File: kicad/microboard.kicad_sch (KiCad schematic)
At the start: 12 parts, among them J2 to microboard, J3 to baseboard, Q1 AH3712-P-B, U3 HT7550, U5 LM35-LP

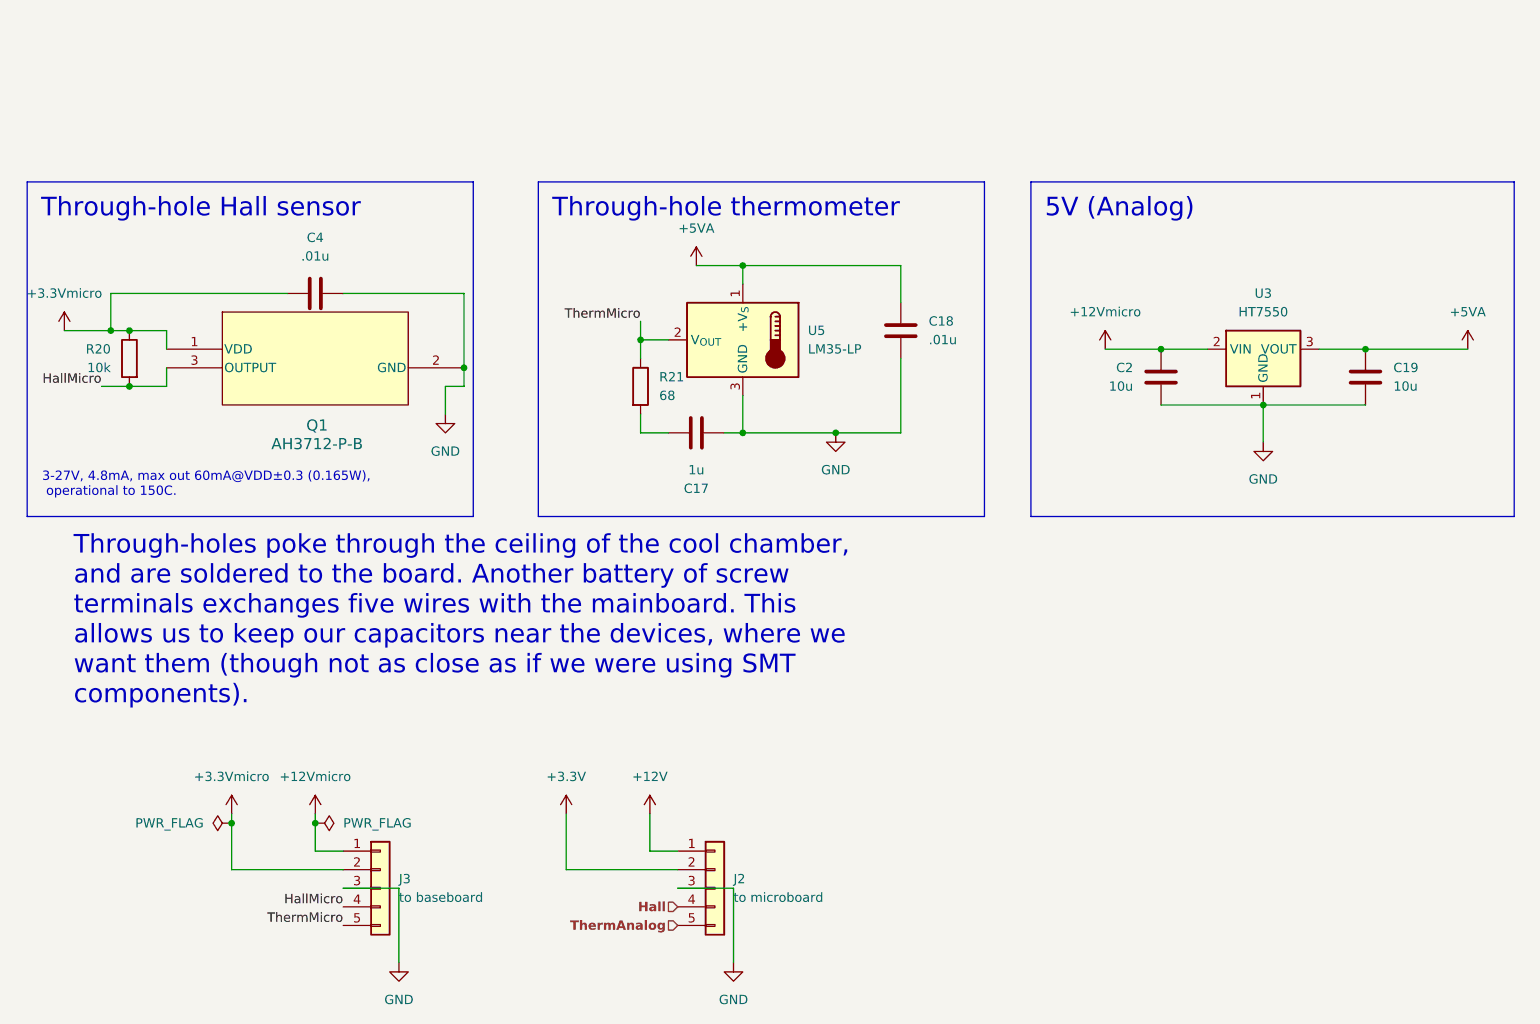
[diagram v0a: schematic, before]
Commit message: call ledc_fade_func_install(). call setup_adc_oneshot() after setup_temp()
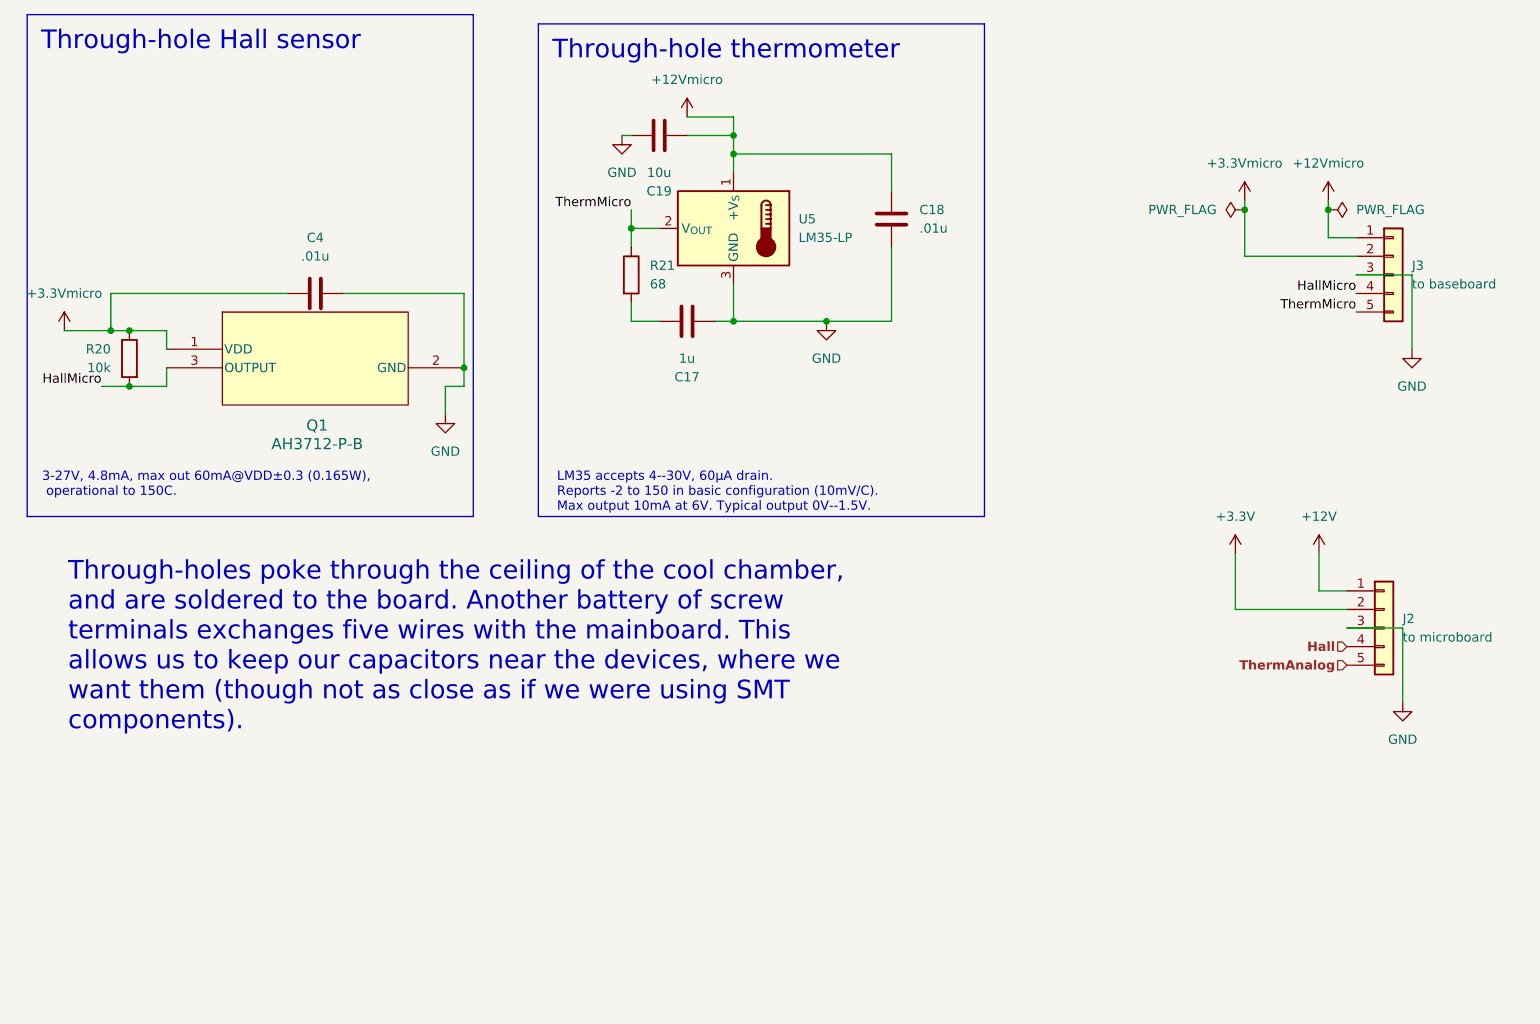
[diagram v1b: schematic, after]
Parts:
- removed C2: 10u, Capacitor_SMD:C_0805_2012Metric_Pad1.18x1.45mm_HandSolder, symbol Device:C
- removed U3: HT7550, Package_TO_SOT_SMD:SOT-89-3, symbol Regulator_Linear:HT75xx-1-SOT89
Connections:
- net +12Vmicro: now also C18.1, C19.2, U5.1 (+V_{S})
- net GND: now also C19.1; no longer C19.2
- removed net +5VA: C18.1, C19.1, U5.1 (+V_{S})
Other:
- note added: "LM35 accepts 4--30V, 60µA drain. Reports -2 to 150 in basic configuration (10mV/C). Max output 10mA at 6V. Typical output 0V--1.5V."
- moved on the sheet: C17, C18, C19, J2, J3, R21, U5

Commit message: [schematics] sync to grid
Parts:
- C18, C4: value .01u -> 10n
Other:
- note added: "Through-holes poke through the ceiling of the cool chamber, and are soldered to the board. A JST connector exchanges five wires with the mainboard. This allows us to keep our capacitors near the devices, where we want them (though not as close as if we were using SMT components)."
- note removed: "Through-holes poke through the ceiling of the cool chamber, and are soldered to the board. Another battery of screw terminals exchanges five wires with the mainboard. This allows us to keep our capacitors near the devices, where we want them (though not as close as if we were using SMT components)."
- moved on the sheet: C17, C18, C19, C4, Q1, R20, R21, U5

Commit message: [kicad] tighten things up
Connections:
- net +3.3V: now also J2.3 (Pin_3); no longer J2.2 (Pin_2)
- net +3.3Vmicro: now also J3.3 (Pin_3); no longer J3.2 (Pin_2)
- net GND: now also J2.2 (Pin_2), J3.2 (Pin_2); no longer J2.3 (Pin_3), J3.3 (Pin_3)

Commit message: put your boot down
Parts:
- C17, C18, C19, C4: footprint Capacitor_SMD:C_0805_2012Metric_Pad1.18x1.45mm_HandSolder -> Capacitor_SMD:C_1206_3216Metric_Pad1.33x1.80mm_HandSolder
- R20, R21: footprint Resistor_SMD:R_0805_2012Metric_Pad1.20x1.40mm_HandSolder -> Resistor_SMD:R_1206_3216Metric_Pad1.30x1.75mm_HandSolder
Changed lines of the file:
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@@
 			)
 		)
-		(property "Footprint" "Resistor_SMD:R_0805_2012Metric_Pad1.20x1.40mm_HandSolder"
+		(property "Footprint" "Resistor_SMD:R_1206_3216Metric_Pad1.30x1.75mm_HandSolder"
 			(at 117.602 71.12 90)
 			(effects
@@
 			)
 		)
-		(property "Footprint" "Resistor_SMD:R_0805_2012Metric_Pad1.20x1.40mm_HandSolder"
+		(property "Footprint" "Resistor_SMD:R_1206_3216Metric_Pad1.30x1.75mm_HandSolder"
 			(at 51.308 63.5 90)
 			(effects
@@
 			)
 		)
-		(property "Footprint" "Capacitor_SMD:C_0805_2012Metric_Pad1.18x1.45mm_HandSolder"
+		(property "Footprint" "Capacitor_SMD:C_1206_3216Metric_Pad1.33x1.80mm_HandSolder"
 			(at 153.9748 67.31 0)
 			(effects
@@
 			)
 		)
-		(property "Footprint" "Capacitor_SMD:C_0805_2012Metric_Pad1.18x1.45mm_HandSolder"
+		(property "Footprint" "Capacitor_SMD:C_1206_3216Metric_Pad1.33x1.80mm_HandSolder"
 			(at 127 53.0352 0)
 			(effects
@@
 			)
 		)
-		(property "Footprint" "Capacitor_SMD:C_0805_2012Metric_Pad1.18x1.45mm_HandSolder"
+		(property "Footprint" "Capacitor_SMD:C_1206_3216Metric_Pad1.33x1.80mm_HandSolder"
 			(at 71.12 53.6448 0)
 			(effects
@@
 			)
 		)
-		(property "Footprint" "Capacitor_SMD:C_0805_2012Metric_Pad1.18x1.45mm_HandSolder"
+		(property "Footprint" "Capacitor_SMD:C_1206_3216Metric_Pad1.33x1.80mm_HandSolder"
 			(at 130.81 78.4352 0)
 			(effects

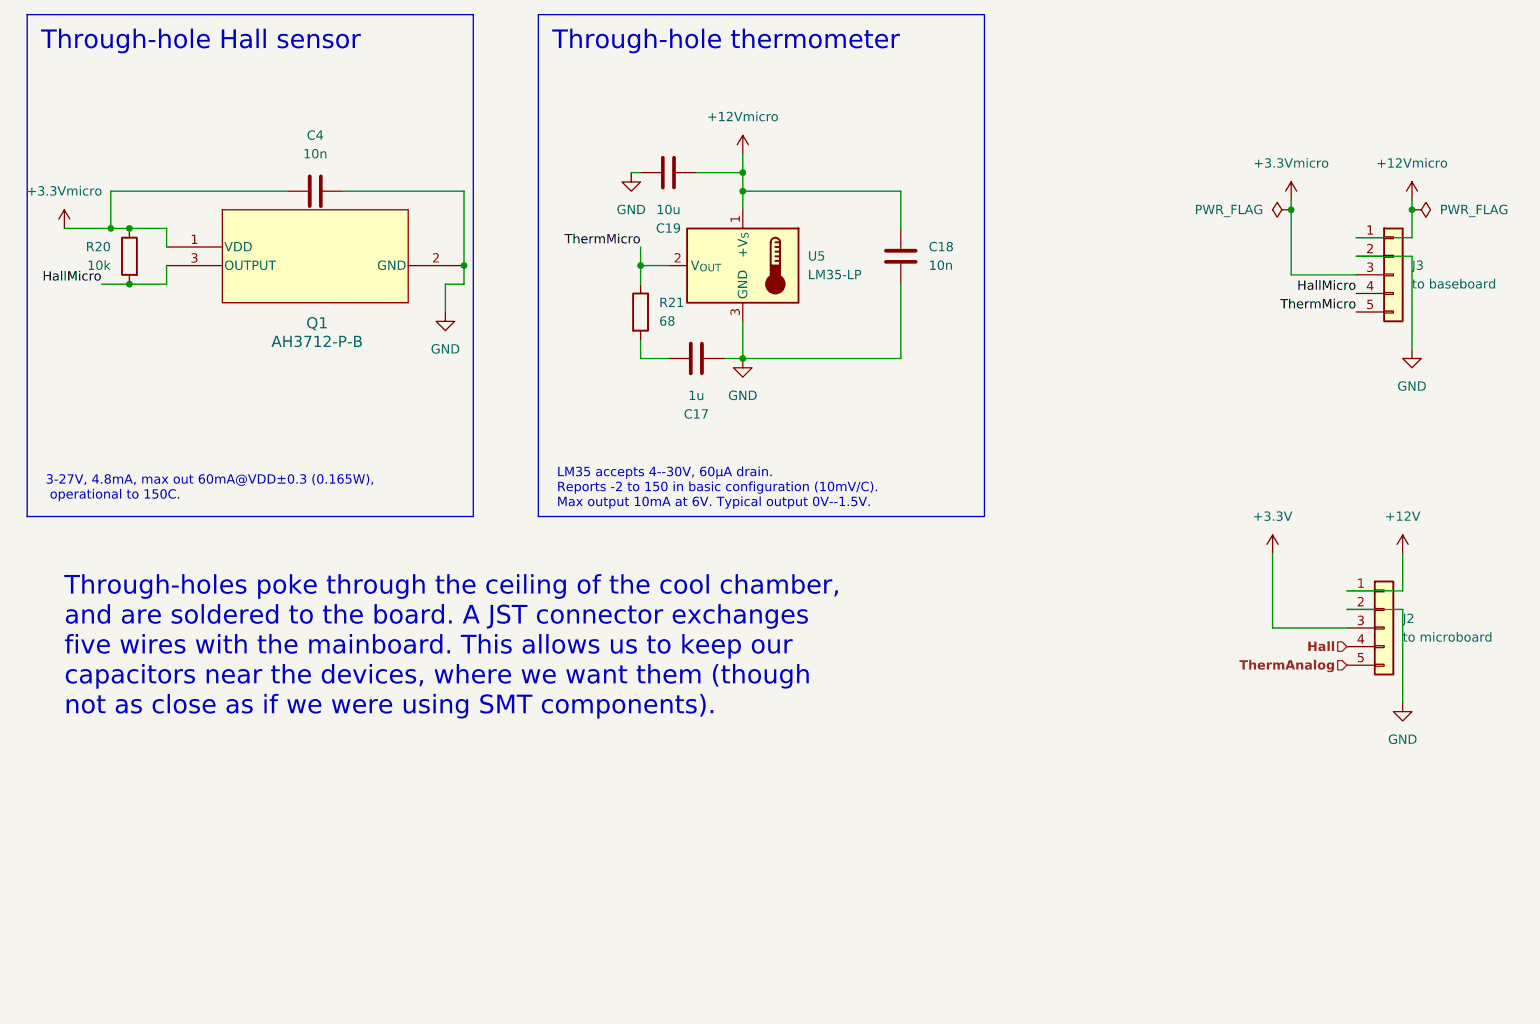
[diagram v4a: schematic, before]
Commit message: move from lm35 to lmt87lpm
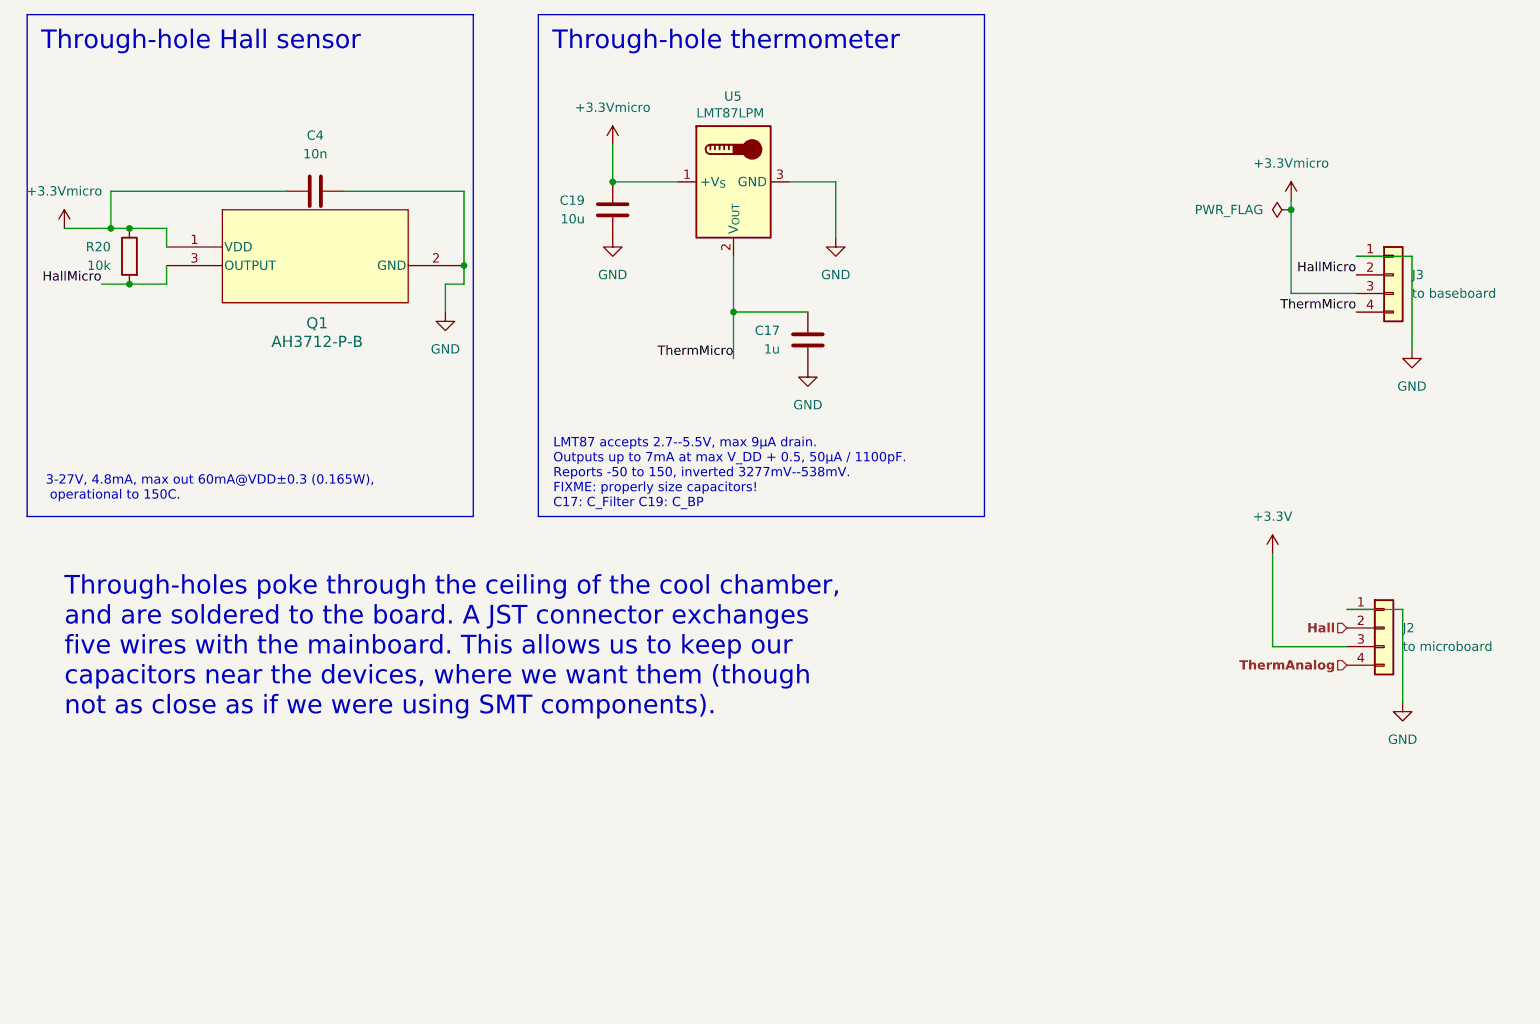
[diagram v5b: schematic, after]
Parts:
- removed C18: 10n, Capacitor_SMD:C_1206_3216Metric_Pad1.33x1.80mm_HandSolder, symbol Device:C
- removed R21: 68, Resistor_SMD:R_1206_3216Metric_Pad1.30x1.75mm_HandSolder, symbol Device:R
- J2, J3: footprint Connector_JST:JST_VH_B5P-VH-B_1x05_P3.96mm_Vertical -> dank:JST_VH_B4P-VH-B_1x04_P3.96mm_Vertical; symbol Connector_Generic:Conn_01x05 -> Connector_Generic:Conn_01x04
- U5: value LM35-LP -> LMT87LPM
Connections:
- net +12V is gone; now on net GND: J2.1 (Pin_1)
- net +3.3Vmicro: now also C19.2, U5.1 (+V_{S})
- net GND: now also C17.1, J3.1 (Pin_1); no longer C17.2, J2.2 (Pin_2), J3.2 (Pin_2)
- net Hall: now also J2.2 (Pin_2); no longer J2.4 (Pin_4)
- net HallMicro: now also J3.2 (Pin_2); no longer J3.4 (Pin_4)
- net ThermAnalog: now also J2.4 (Pin_4); no longer J2.5 (Pin_5)
- net ThermMicro: now also C17.2, J3.4 (Pin_4); no longer J3.5 (Pin_5)
- removed net +12Vmicro: C19.2, J3.1 (Pin_1), U5.1 (+V_{S})
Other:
- note added: "LMT87 accepts 2.7--5.5V, max 9µA drain. Outputs up to 7mA at max V_DD + 0.5, 50µA / 1100pF. Reports -50 to 150, inverted 3277mV--538mV. FIXME: properly size capacitors! C17: C_Filter C19: C_BP"
- note removed: "LM35 accepts 4--30V, 60µA drain. Reports -2 to 150 in basic configuration (10mV/C). Max output 10mA at 6V. Typical output 0V--1.5V."
- moved on the sheet: C17, C19, U5
